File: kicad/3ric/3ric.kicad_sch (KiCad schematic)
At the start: 19 parts, among them U1 74LS154, U2 6502-library_65C02S-2, U8 EB6502_isc61c1024-15n

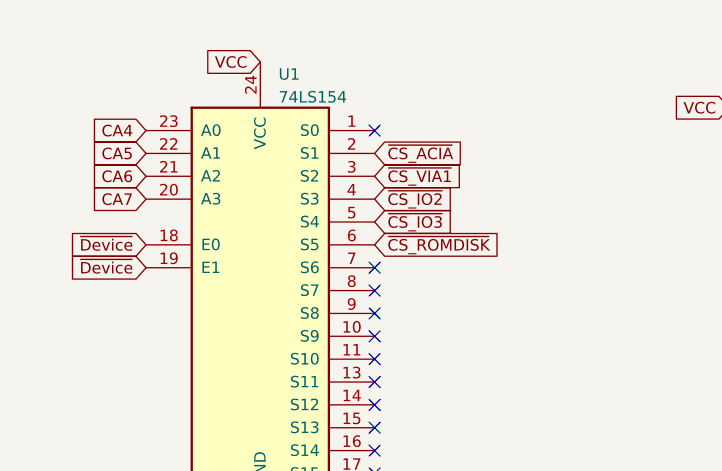
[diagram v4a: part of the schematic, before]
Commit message: move some of the logic to PLD, move device range from C1XX to CX00 update device labels to be more correct update PLD
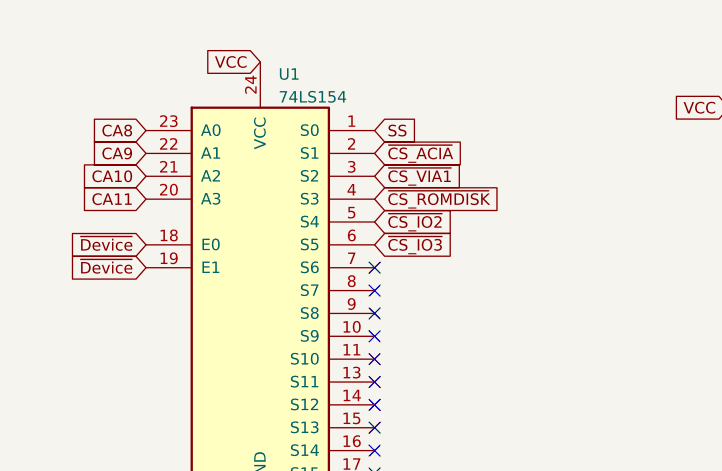
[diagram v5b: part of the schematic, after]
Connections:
- net CA10: now also U1.21 (A2)
- net CA11: now also U1.20 (A3)
- net CA4: no longer U1.23 (A0)
- net CA5: no longer U1.22 (A1)
- net CA6: no longer U1.21 (A2)
- net CA7: no longer U1.20 (A3)
- net CA8: now also U1.23 (A0)
- net CA9: now also U1.22 (A1)
- net ~{CS_IO2}: now also U1.5 (S4); no longer U1.4 (S3)
- net ~{CS_IO3}: now also U1.6 (S5); no longer U1.5 (S4)
- net ~{CS_ROMDISK}: now also U1.4 (S3); no longer U1.6 (S5)
- net SS: now reaches U1.1 (S0)
- no-connect marks 18 -> 17
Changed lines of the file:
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@@
   (no_connect (at 105.41 36.83))
   (no_connect (at 130.81 24.13))
-  (no_connect (at 49.53 26.67))
   (no_connect (at 49.53 46.99))
   (no_connect (at 49.53 44.45))
@@
     )
   )
+  (global_label "~{CS_ROMDISK}" (shape input) (at 49.53 34.29 0) (fields_autoplaced)
+    (effects (font (size 1.27 1.27)) (justify left))
+    (property "Intersheet References" "${INTERSHEET_REFS}" (id 0) (at -173.99 -17.78 0)
+      (effects (font (size 1.27 1.27)) hide)
+    )
+  )
   (global_label "CA11" (shape input) (at 199.39 81.28 0) (fields_autoplaced)
     (effects (font (size 1.27 1.27)) (justify left))
@@
     )
   )
-  (global_label "CA4" (shape input) (at 24.13 26.67 180) (fields_autoplaced)
+  (global_label "CA8" (shape input) (at 24.13 26.67 180) (fields_autoplaced)
     (effects (font (size 1.27 1.27)) (justify right))
     (property "Intersheet References" "${INTERSHEET_REFS}" (id 0) (at 18.1488 26.5906 0)
@@
     )
   )
-  (global_label "~{CS_IO2}" (shape input) (at 49.53 34.29 0) (fields_autoplaced)
-    (effects (font (size 1.27 1.27)) (justify left))
-    (property "Intersheet References" "${INTERSHEET_REFS}" (id 0) (at 58.535 34.2106 0)
-      (effects (font (size 1.27 1.27)) (justify left) hide)
-    )
-  )
   (global_label "VA12" (shape input) (at 173.99 83.82 180) (fields_autoplaced)
     (effects (font (size 1.27 1.27)) (justify right))
@@
     )
   )
-  (global_label "~{CS_IO3}" (shape input) (at 49.53 36.83 0) (fields_autoplaced)
-    (effects (font (size 1.27 1.27)) (justify left))
-    (property "Intersheet References" "${INTERSHEET_REFS}" (id 0) (at 58.535 36.7506 0)
-      (effects (font (size 1.27 1.27)) (justify left) hide)
-    )
-  )
   (global_label "~{CS_RAM}" (shape input) (at 132.08 180.34 0) (fields_autoplaced)
     (effects (font (size 1.27 1.27)) (justify left))
@@
     )
   )
-  (global_label "CA5" (shape input) (at 24.13 29.21 180) (fields_autoplaced)
+  (global_label "CA9" (shape input) (at 24.13 29.21 180) (fields_autoplaced)
     (effects (font (size 1.27 1.27)) (justify right))
     (property "Intersheet References" "${INTERSHEET_REFS}" (id 0) (at 18.1488 29.1306 0)
@@
     )
   )
-  (global_label "~{CS_ROMDISK}" (shape input) (at 49.53 39.37 0) (fields_autoplaced)
-    (effects (font (size 1.27 1.27)) (justify left))
-    (property "Intersheet References" "${INTERSHEET_REFS}" (id 0) (at -173.99 -12.7 0)
-      (effects (font (size 1.27 1.27)) hide)
-    )
-  )
   (global_label "CA15" (shape input) (at 130.81 59.69 0) (fields_autoplaced)
     (effects (font (size 1.27 1.27)) (justify left))
@@
     )
   )
-  (global_label "CA7" (shape input) (at 24.13 34.29 180) (fields_autoplaced)
-    (effects (font (size 1.27 1.27)) (justify right))
-    (property "Intersheet References" "${INTERSHEET_REFS}" (id 0) (at 18.1488 34.2106 0)
+  (global_label "CA11" (shape input) (at 24.13 34.29 180) (fields_autoplaced)
+    (effects (font (size 1.27 1.27)) (justify right))
+    (property "Intersheet References" "${INTERSHEET_REFS}" (id 0) (at 16.9393 34.2106 0)
       (effects (font (size 1.27 1.27)) (justify right) hide)
     )
@@
     )
   )
+  (global_label "~{CS_IO3}" (shape input) (at 49.53 39.37 0) (fields_autoplaced)
+    (effects (font (size 1.27 1.27)) (justify left))
+    (property "Intersheet References" "${INTERSHEET_REFS}" (id 0) (at 58.535 39.2906 0)
+      (effects (font (size 1.27 1.27)) (justify left) hide)
+    )
+  )
   (global_label "CD5" (shape input) (at 130.81 52.07 0) (fields_autoplaced)
     (effects (font (size 1.27 1.27)) (justify left))
@@
     )
   )
-  (global_label "CA6" (shape input) (at 24.13 31.75 180) (fields_autoplaced)
-    (effects (font (size 1.27 1.27)) (justify right))
-    (property "Intersheet References" "${INTERSHEET_REFS}" (id 0) (at 18.1488 31.6706 0)
+  (global_label "CA10" (shape input) (at 24.13 31.75 180) (fields_autoplaced)
+    (effects (font (size 1.27 1.27)) (justify right))
+    (property "Intersheet References" "${INTERSHEET_REFS}" (id 0) (at 16.9393 31.6706 0)
       (effects (font (size 1.27 1.27)) (justify right) hide)
     )
@@
     )
   )
+  (global_label "SS" (shape input) (at 49.53 26.67 0) (fields_autoplaced)
+    (effects (font (size 1.27 1.27)) (justify left))
+    (property "Intersheet References" "${INTERSHEET_REFS}" (id 0) (at 54.3621 26.5906 0)
+      (effects (font (size 1.27 1.27)) (justify left) hide)
+    )
+  )
   (global_label "CD0" (shape input) (at 173.99 120.65 180) (fields_autoplaced)
     (effects (font (size 1.27 1.27)) (justify right))
@@
     (property "Intersheet References" "${INTERSHEET_REFS}" (id 0) (at 99.4893 116.7606 0)
       (effects (font (size 1.27 1.27)) (justify right) hide)
+    )
+  )
+  (global_label "~{CS_IO2}" (shape input) (at 49.53 36.83 0) (fields_autoplaced)
+    (effects (font (size 1.27 1.27)) (justify left))
+    (property "Intersheet References" "${INTERSHEET_REFS}" (id 0) (at 58.535 36.7506 0)
+      (effects (font (size 1.27 1.27)) (justify left) hide)
     )
   )
@@
       (reference "U?") (unit 1) (value "74LS32") (footprint "")
     )
-    (path "/b718fcb1-8742-4b46-85e8-c35e05bc00ea/75180dec-5a3c-4561-bdef-7e8bed61e3e4"
-      (reference "U?") (unit 1) (value "74LS00") (footprint "")
-    )
-    (path "/b718fcb1-8742-4b46-85e8-c35e05bc00ea/7832474f-7073-4a75-95f9-2c0a0280bb7d"
-      (reference "U?") (unit 1) (value "74LS08") (footprint "")
-    )
-    (path "/b718fcb1-8742-4b46-85e8-c35e05bc00ea/7cc70384-b819-4a3a-bda9-38dbf422a209"
-      (reference "U?") (unit 1) (value "74LS32") (footprint "")
-    )
     (path "/b718fcb1-8742-4b46-85e8-c35e05bc00ea/82a84490-7a3d-4fcd-ab1a-7a15ec393dce"
       (reference "U?") (unit 1) (value "74LS32") (footprint "")
@@
       (reference "U?") (unit 1) (value "74LS00") (footprint "")
     )
-    (path "/b718fcb1-8742-4b46-85e8-c35e05bc00ea/f03461a1-307c-4bfd-90e3-831641123f03"
-      (reference "U?") (unit 1) (value "74LS14") (footprint "")
-    )
     (path "/817a35a7-de63-4412-ae79-57fde5eabc67/f5612141-8816-4767-b72d-d83561b9f378"
       (reference "U?") (unit 1) (value "6502-library_65C51N") (footprint "Package_DIP:DIP-28_W15.24mm_Socket")
@@
       (reference "U?") (unit 2) (value "74LS00") (footprint "")
     )
-    (path "/b718fcb1-8742-4b46-85e8-c35e05bc00ea/37f37914-e8e7-48b3-9784-24b435a1454c"
-      (reference "U?") (unit 2) (value "74LS08") (footprint "")
-    )
     (path "/c920751f-edd2-4cd3-a630-9d0b3423e6d7/3ae6f5e8-b451-4dbf-960f-4ea76e72affc"
       (reference "U?") (unit 2) (value "74LS32") (footprint "")
@@
       (reference "U?") (unit 2) (value "74LS32") (footprint "")
     )
-    (path "/b718fcb1-8742-4b46-85e8-c35e05bc00ea/4275474c-4f83-4af8-bf2f-80f5e61aaee2"
-      (reference "U?") (unit 2) (value "74LS00") (footprint "")
-    )
     (path "/b718fcb1-8742-4b46-85e8-c35e05bc00ea/6dd49738-c493-4f2a-bd98-72d7cde751fa"
       (reference "U?") (unit 2) (value "74LS32") (footprint "")
@@
       (reference "U?") (unit 2) (value "74LS112") (footprint "")
     )
-    (path "/b718fcb1-8742-4b46-85e8-c35e05bc00ea/964c995a-324f-4dee-ac50-1e1bf6d23794"
-      (reference "U?") (unit 2) (value "74LS32") (footprint "")
-    )
     (path "/b718fcb1-8742-4b46-85e8-c35e05bc00ea/971eb0ac-e5bb-46c0-9b46-853c2856a9e4"
       (reference "U?") (unit 2) (value "74LS32") (footprint "")
@@
       (reference "U?") (unit 2) (value "74LS11") (footprint "")
     )
-    (path "/b718fcb1-8742-4b46-85e8-c35e05bc00ea/d1a2607c-d858-46ff-8864-fc1e174ad9b2"
-      (reference "U?") (unit 2) (value "74LS14") (footprint "")
-    )
     (path "/c920751f-edd2-4cd3-a630-9d0b3423e6d7/d4b00acd-89ed-422d-83e9-93b327d5d3f7"
       (reference "U?") (unit 2) (value "74LS00") (footprint "")
@@
       (reference "U?") (unit 3) (value "74LS32") (footprint "")
     )
-    (path "/b718fcb1-8742-4b46-85e8-c35e05bc00ea/41cd2e8d-e3fe-4641-9086-afb50d496e5a"
-      (reference "U?") (unit 3) (value "74LS32") (footprint "")
-    )
     (path "/c920751f-edd2-4cd3-a630-9d0b3423e6d7/4b4e1178-67f9-482d-bba7-fcbd867f54e6"
       (reference "U?") (unit 3) (value "74LS32") (footprint "")
     )
-    (path "/b718fcb1-8742-4b46-85e8-c35e05bc00ea/60b5afc2-8c6f-4700-89cc-4758ab35b881"
-      (reference "U?") (unit 3) (value "74LS32") (footprint "")
-    )

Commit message: push schematic updates
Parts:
- removed R1, R2, R3, R4, R? (x2): 1K, Resistor_THT:R_Axial_DIN0207_L6.3mm_D2.5mm_P7.62mm_Horizontal, symbol Device:R
- removed U1: 74LS154, Package_DIP:DIP-24_W15.24mm_Socket, symbol 74xx:74LS154
- removed U2: 6502-library_65C02S-2, Package_DIP:DIP-40_W15.24mm_Socket, symbol EB6502-custom:6502-library_65C02S-2
- removed U8: EB6502_isc61c1024-15n, Package_DIP:DIP-32_W7.62mm, symbol EB6502-cache:EB6502_isc61c1024-15n
- removed U?: 74LS11, symbol 74xx:74LS11
- removed U_BUS_A_HIGH1, U_BUS_A_LOW_1, U_BUS_DATA_1: 74LS245, Package_DIP:DIP-20_W7.62mm_Socket, symbol 74xx:74LS245
- removed U_DECODER_PLD1: 22V10C, Package_DIP:DIP-24_W7.62mm_Socket, symbol 6502:22V10C
- removed U_ROM: SST39SF040, Package_DIP:DIP-32_W15.24mm_Socket, symbol Memory_Flash:SST39SF040
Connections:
- no-connect marks 17 -> 0
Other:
- sheet Communication renamed Devices, Serial, VIA
- sheet banking renamed Language Card and Sound
- sheet vga_memsignal renamed Clock signals
- sheet vga_vidmem renamed Video address and counters
- sheet vgatiming renamed Clock and VGA signals
- removed sheet pixels
- added sheet GraphicsV2 (graphicsv2.kicad_sch)
- added sheet LowRes (LowRes.kicad_sch)
- added sheet Mockingboard (Mockingboard.kicad_sch)
- added sheet Power2 (power2.kicad_sch)
- added sheet RAM (ram.kicad_sch)
- added sheet SoftSwitches (softswitches.kicad_sch)
- added sheet TextMode (text.kicad_sch)
- added sheet cpu_rom (cpu_rom.kicad_sch)
- note added: "3RIC 2/21/2024"
